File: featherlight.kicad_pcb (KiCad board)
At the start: 4 copper layers, 88.9 x 88.9 mm, 84 parts, among them IC1 BNO055, P1 USB_OTG, P10 CONN_01X06, P11 CONN_01X06, P12 CONN_01X06, P13 CONN_01X06, P14 CONN_01X06, P15 CONN_01X06, P16 CONN_01X06, P17 CONN_01X01, P18 CONN_01X01, P2 CONN_01X06, P3 CONN_01X06, P4 CONN_01X06, P5 CONN_01X06, P6 CONN_01X06, P7 CONN_01X06, P8 CONN_01X06, P9 CONN_01X06, SW1 SW_PUSH_SMALL_H, U1 74AHCT1G125, U2 SAMD21G18A-A, U3 AP2112, Y1 32.768 KHz, Y2 32.768 KHz

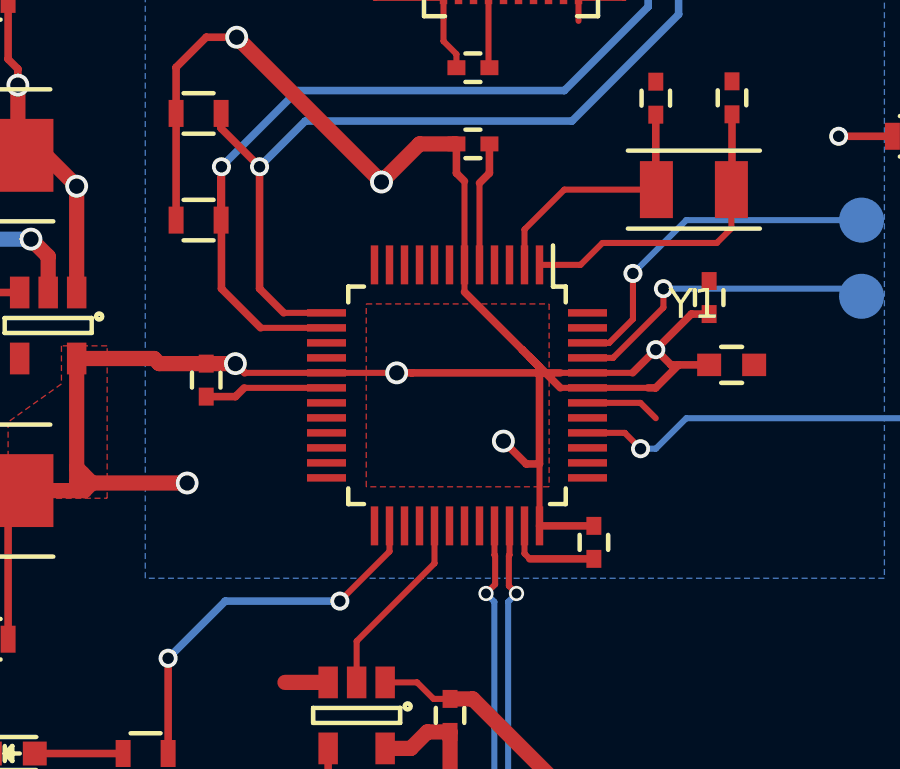
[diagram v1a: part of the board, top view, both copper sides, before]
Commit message: Component changes to reduce BOM cost.
-Swap SAMD21 package to 48-QFN.
-Swap Tantalum power caps for Aluminum Polymer.
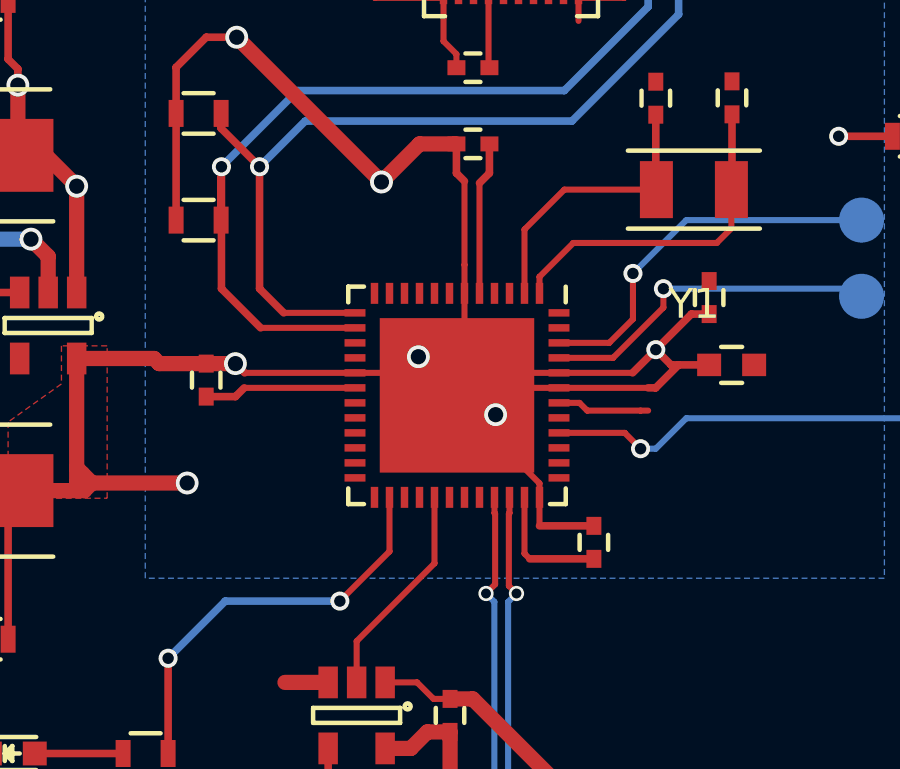
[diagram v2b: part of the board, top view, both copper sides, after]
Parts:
- C17, C18: value 100 uF -> 220 uF
- R2: value 100K -> 100 K
- R3, R4: value R_Small -> 10 K
- R6, R8: value 150 -> 1 K
- R7: value 330 -> 1 K
- SW1: value SW_PUSH_SMALL_H -> Button
- U2: value SAMD21G18A-A -> SAMD21G18; footprint Housings_QFP:TQFP-48_7x7mm_Pitch0.5mm -> Housings_DFN_QFN:QFN-48-1EP_7x7mm_Pitch0.5mm
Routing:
- net +3V3: track 95.4 -> 115.2 mm
- net GND: track 169.8 -> 173.2 mm
- net Net-(U1-Pad2): track 6.29 -> 7.24 mm
- net Net-(R6-Pad2): track 12.9 -> 13.8 mm
- net Net-(C24-Pad2): track 8.63 -> 9.58 mm
- net D-: track 18.4 -> 19.4 mm
- net D+: track 18.4 -> 19.4 mm
- net /MCU + IMU/~RST~: track 31.8 -> 32.7 mm
- net /MCU + IMU/SWDIO: track 11.7 -> 12.7 mm
- net /MCU + IMU/SWCLK: track 10.6 -> 11.5 mm
- net /MCU + IMU/SDA: track 32.2 -> 33.2 mm
- net /MCU + IMU/SCL: track 31.2 -> 32.2 mm
- net Net-(C23-Pad2): track 10.7 -> 11.4 mm
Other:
- board text added: "Featherlight Prototype Rev B"
- board text removed: "Featherlight Prototype Rev A"

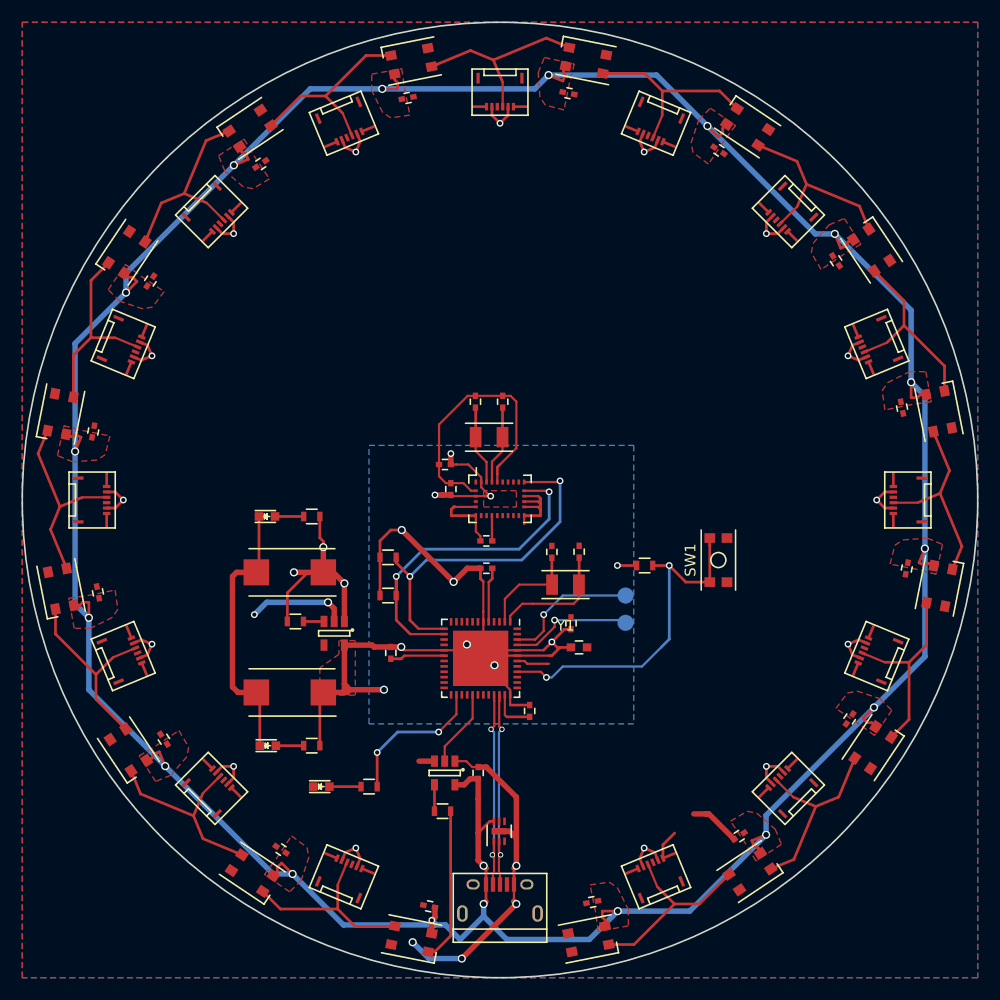
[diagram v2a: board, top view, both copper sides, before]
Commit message: Further development work while waiting for the first prototypes to come back.
-Moved to 4 layer board because the power routing got to be too much of a headache.
-Run all power through a PTC fuse.
-Added a voltage divider to allow the MCU to monitor bus voltage.
-Added JST-2 connector and battery circuitry to permit powering from lipo cells.  Feeds VDD via a diode to avoid bad things happening.  Intended to work with Adafruit's packs.
-Added 4 push buttons to form a user interface.
-Removed external pull up resistor on reset line.  MCU has internal pull ups.
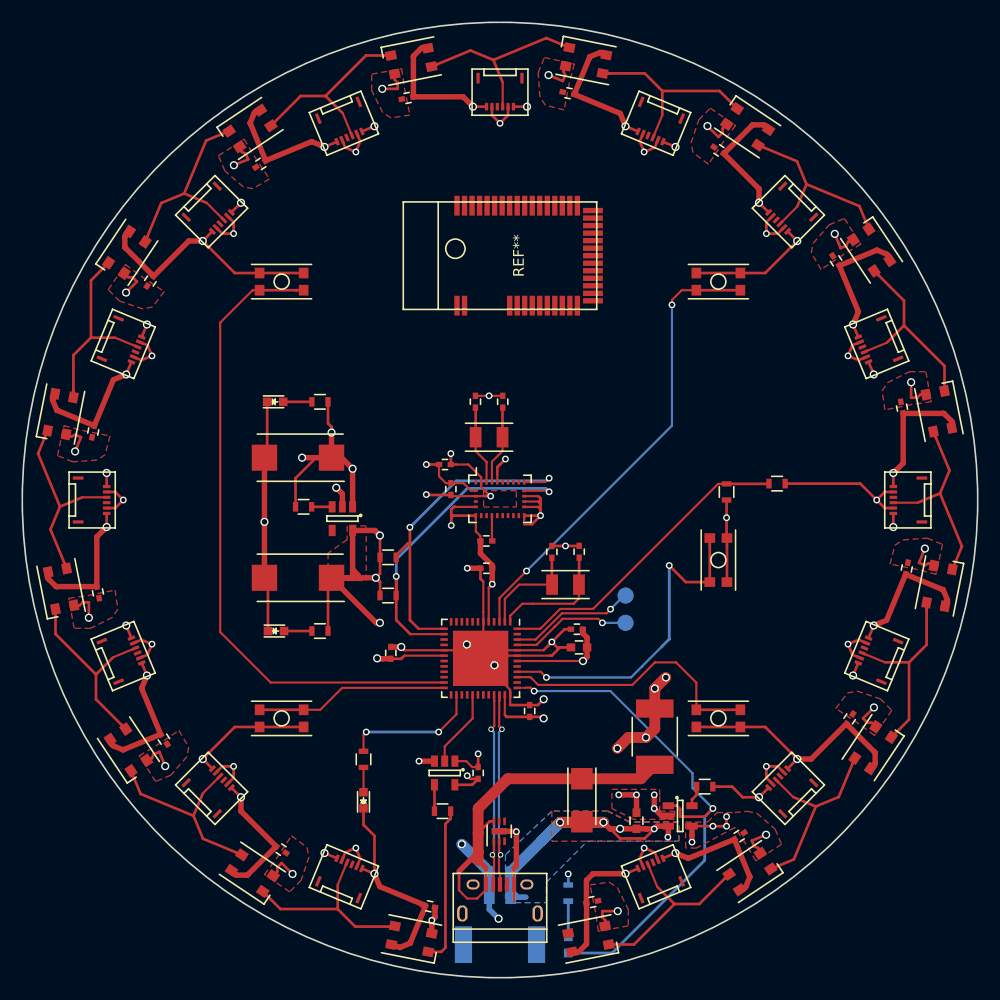
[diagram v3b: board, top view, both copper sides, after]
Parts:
- added C32: 4.7 uF, Capacitors_SMD:C_0603, F.Cu at (114.3, 131.4)
- added D21: D_Schottky, featherlight:DO-214AC, F.Cu at (109.2, 129.5)
- added D22: Green, LEDs:LED_0603, B.Cu at (108.0, 143.0)
- added F1: FUSE, featherlight:1812_PTC, F.Cu at (116.0, 123.6)
- added P19: CONN_01X02, Connectors_JST:JST_PH_S2B-PH-SM4-TB_02x2.00mm_Angled, B.Cu at (101.6, 140.2)
- added R10: 10 K, Resistors_SMD:R_0603, F.Cu at (120.7, 128.3)
- added R11: 100 K, Resistors_SMD:R_0603, F.Cu at (122.7, 100.8)
- added R9: 470, Resistors_SMD:R_0603, B.Cu at (108.0, 138.2)
- added REF**: MDBT40, featherlight:MDBT40, F.Cu at (101.6, 78.9)
- added SW2: Button, featherlight:KMR2_switch, F.Cu at (81.3, 81.3)
- added SW3: Button, featherlight:KMR2_switch, F.Cu at (121.9, 81.3)
- added SW4: Button, featherlight:KMR2_switch, F.Cu at (81.3, 121.9)
- added SW5: Button, featherlight:KMR2_switch, F.Cu at (121.9, 121.9)
- added U4: MCP73831, TO_SOT_Packages_SMD:SOT-23-5, F.Cu at (118.4, 131.0)
- moved R5 14.5 mm to (127.4, 100.1)
- moved C17 10.7 mm to (82.8, 97.7)
- moved C18 10.7 mm to (82.8, 108.8)
- moved D19 10.7 mm to (80.7, 92.5)
- moved R2 10.7 mm to (83.3, 102.2)
- moved R7 10.7 mm to (84.8, 92.5)
- moved U3 10.7 mm to (86.9, 103.3)
- moved D20 10.7 mm to (80.8, 113.8)
- moved R8 10.7 mm to (84.8, 113.8)
- moved D18 4.12 mm to (88.9, 129.5), turned to 90 degrees
- moved R6 2.59 mm to (88.9, 125.7), turned to 90 degrees
- moved C25 0.78 mm to (108.8, 113.6), turned to 0 degrees
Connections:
- net REG_ENABLE renamed Net-(R2-Pad1)
- C1 pad 1: +5V -> VDD
- C10 pad 1: +5V -> VDD
- C11 pad 1: +5V -> VDD
- C12 pad 1: +5V -> VDD
- C13 pad 1: +5V -> VDD
- C14 pad 1: +5V -> VDD
- C15 pad 1: +5V -> VDD
- C16 pad 1: +5V -> VDD
- C17 pad 1: +5V -> VDD
- C2 pad 1: +5V -> VDD
- C3 pad 1: +5V -> VDD
- C31 pad 1: +5V -> VDD
- C4 pad 1: +5V -> VDD
- C5 pad 1: +5V -> VDD
- C6 pad 1: +5V -> VDD
- C7 pad 1: +5V -> VDD
- C8 pad 1: +5V -> VDD
- C9 pad 1: +5V -> VDD
- D1 pad 4: +5V -> VDD
- D10 pad 4: +5V -> VDD
- D11 pad 4: +5V -> VDD
- D12 pad 4: +5V -> VDD
- D13 pad 4: +5V -> VDD
- D14 pad 4: +5V -> VDD
- D15 pad 4: +5V -> VDD
- D16 pad 4: +5V -> VDD
- D17 pad 6: +5V -> VUSB
- D2 pad 4: +5V -> VDD
- D3 pad 4: +5V -> VDD
- D4 pad 4: +5V -> VDD
- D5 pad 4: +5V -> VDD
- D6 pad 4: +5V -> VDD
- D7 pad 4: +5V -> VDD
- D8 pad 4: +5V -> VDD
- D9 pad 4: +5V -> VDD
- P1 pad 1: +5V -> VUSB
- P10 pad 2: +5V -> VDD
- P10 pad 5: +5V -> VDD
- P11 pad 2: +5V -> VDD
- P11 pad 5: +5V -> VDD
- P12 pad 2: +5V -> VDD
- P12 pad 5: +5V -> VDD
- P13 pad 2: +5V -> VDD
- P13 pad 5: +5V -> VDD
- P14 pad 2: +5V -> VDD
- P14 pad 5: +5V -> VDD
- P15 pad 2: +5V -> VDD
- P15 pad 5: +5V -> VDD
- P16 pad 2: +5V -> VDD
- P16 pad 5: +5V -> VDD
- P2 pad 2: +5V -> VDD
- P2 pad 5: +5V -> VDD
- P3 pad 2: +5V -> VDD
- P3 pad 5: +5V -> VDD
- P4 pad 2: +5V -> VDD
- P4 pad 5: +5V -> VDD
- P5 pad 2: +5V -> VDD
- P5 pad 5: +5V -> VDD
- P6 pad 2: +5V -> VDD
- P6 pad 5: +5V -> VDD
- P7 pad 2: +5V -> VDD
- P7 pad 5: +5V -> VDD
- P8 pad 2: +5V -> VDD
- P8 pad 5: +5V -> VDD
- P9 pad 2: +5V -> VDD
- P9 pad 5: +5V -> VDD
- R2 pad 2: +5V -> VDD
- R5 pad 1: +3V3 -> VDD_MON
- R5 pad 2: /MCU + IMU/~RST~ -> VDD
- R7 pad 1: +5V -> VDD
- U1 pad 5: +5V -> VDD
- U2 pad 23: (no net) -> /MCU + IMU/UL_BUTTON
- U2 pad 24: (no net) -> /MCU + IMU/LL_BUTTON
- U2 pad 3: (no net) -> /MCU + IMU/UR_BUTTON
- U2 pad 37: (no net) -> CHARGE_STATUS
- U2 pad 39: (no net) -> /MCU + IMU/LR_BUTTON
- U2 pad 48: (no net) -> VDD_MON
- U3 pad 1: +5V -> VDD
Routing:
- net +5V: track 406.2 -> 0.00 mm, vias 36 -> 0
- net GND: track 173.2 -> 395.7 mm, vias 6 -> 52
- net VDD: track 0.00 -> 152.1 mm, vias 0 -> 44
- net /MCU + IMU/UL_BUTTON: track 0.00 -> 60.6 mm
- net CHARGE_STATUS: track 0.00 -> 50.4 mm, vias 0 -> 2
- net /MCU + IMU/UR_BUTTON: track 0.00 -> 43.3 mm, vias 0 -> 2
- net VUSB: track 0.00 -> 35.4 mm
- net +BATT: track 0.00 -> 33.7 mm, vias 0 -> 5
- net VDD_MON: track 0.00 -> 29.0 mm
- net /MCU + IMU/LR_BUTTON: track 0.00 -> 25.2 mm
- net /MCU + IMU/LL_BUTTON: track 0.00 -> 18.0 mm
- net +3V3: track 115.2 -> 110.9 mm, vias 11 -> 12
- net Net-(D22-Pad2): track 0.00 -> 3.33 mm
- net Net-(R10-Pad1): track 0.00 -> 1.96 mm
- net /MCU + IMU/~RST~: track 32.7 -> 31.2 mm
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- added copper zone on Split_Power, net +3V3
- added copper zone on B.Cu, net +BATT
- added copper zone on F.Cu, net +BATT
- added copper zone on Gnd, net GND
- added copper zone on F.Cu, net VDD
- added copper zone on Split_Power, net VDD
- removed copper zone on B.Cu, net +3V3
- removed copper zone on B.Cu, net +5V
- removed copper zone on F.Cu, net +5V

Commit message: Tweaked trace routing to remove several vias.
Expanded the copper pour connecting 3.3V regulator to power plane.
Removed placeholder MDBT40 footprint.  I want to see if the buttons are enough of a UI that bluetooth is no longer necessary.
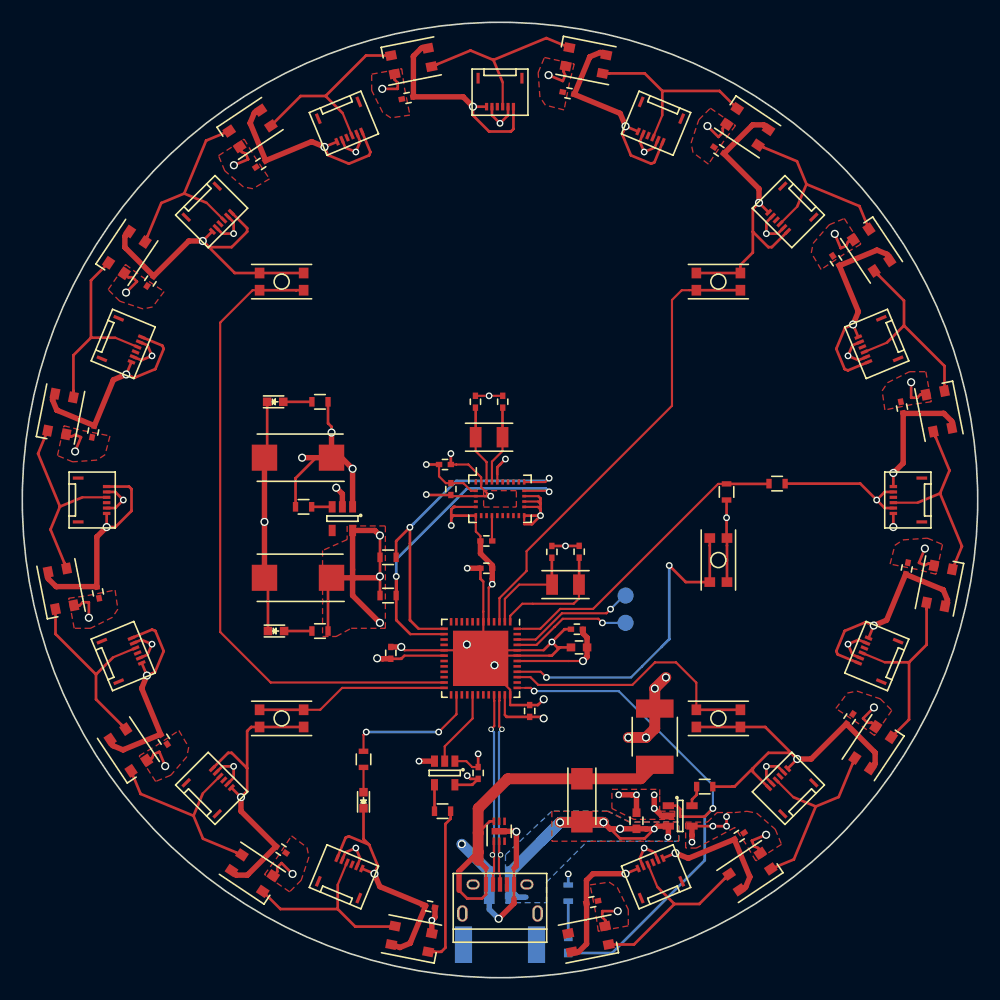
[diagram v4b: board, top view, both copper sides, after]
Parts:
- removed REF**: MDBT40, featherlight:MDBT40
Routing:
- net GND: track 395.7 -> 470.2 mm, vias 52 -> 39
- net +3V3: track 110.9 -> 106.6 mm
- net VDD: track 152.1 -> 150.7 mm
- net /MCU + IMU/SDA: track 31.9 -> 33.0 mm
- net /MCU + IMU/UR_BUTTON: vias 2 -> 0
